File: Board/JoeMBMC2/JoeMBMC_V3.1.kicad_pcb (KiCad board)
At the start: 2 copper layers, 68 x 92 mm, 73 parts, among them J1 5007620481, J2 CAN2_T, J3 CAN1_T, Q1 BSO615NG, Q2 BSO615NG, Q3 P-Chanel Mosfet, U1 Teensy4.0, U2 SN65HVD230, U3 DCDC 5V, U4 IS281-4, U5 SN65HVD230, U6 DCDC 3.3V, U7 Level Shifter 5V to 3V, U8 Level Shifter 5V to 3V

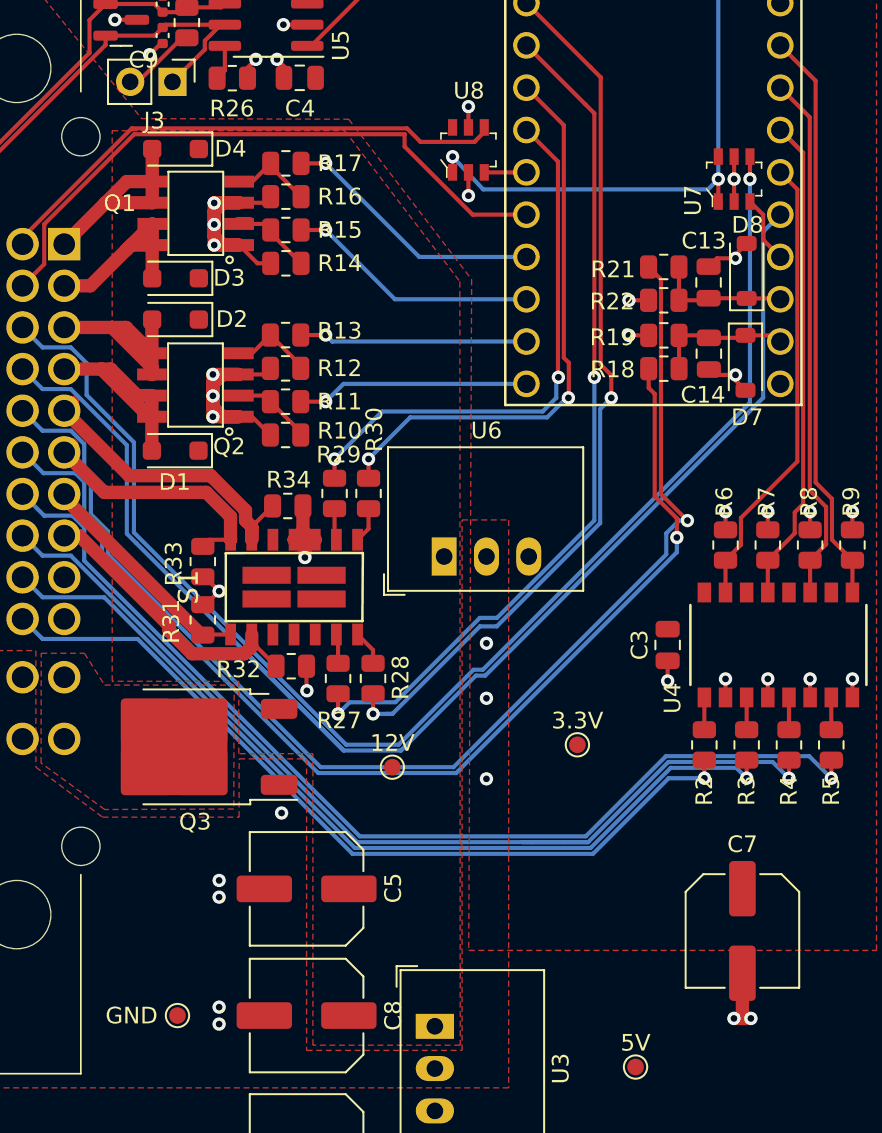
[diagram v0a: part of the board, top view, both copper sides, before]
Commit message: remove zener on analogue sensor inputs
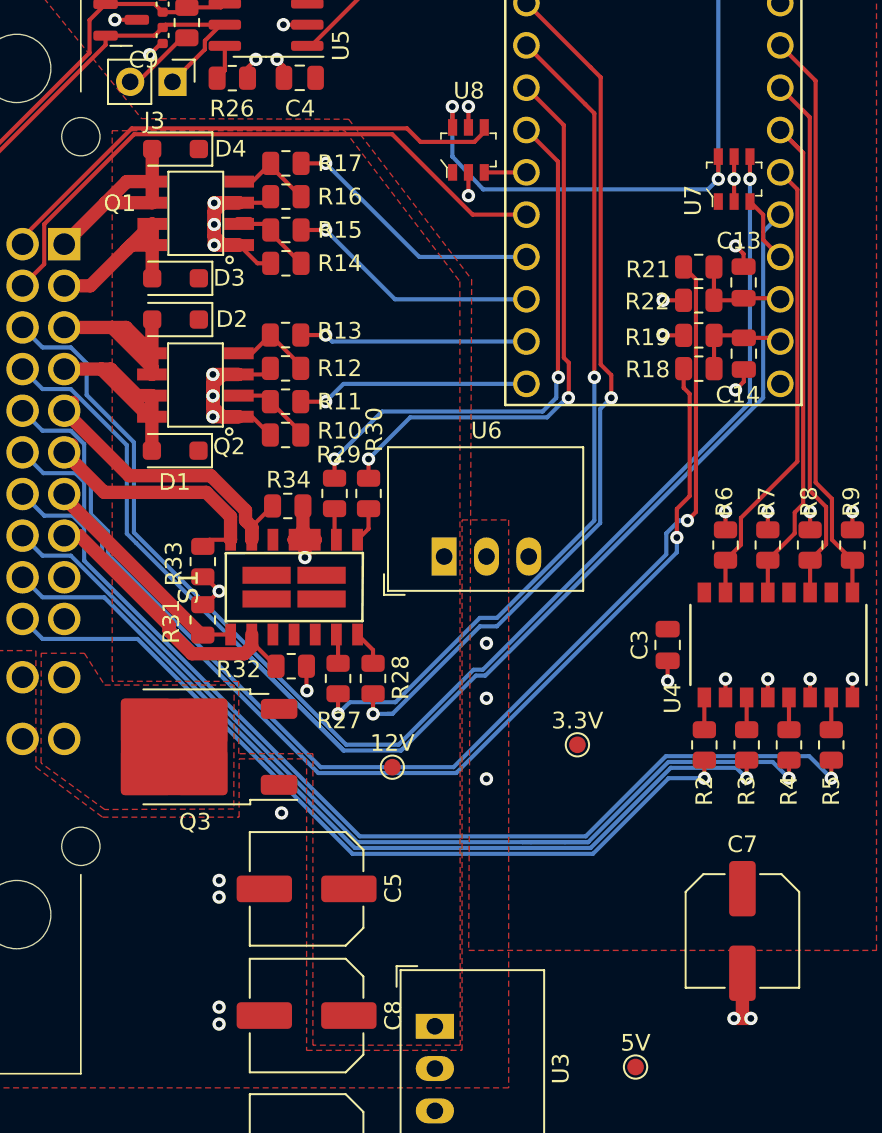
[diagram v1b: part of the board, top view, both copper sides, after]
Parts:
- removed D7, D8: D_Zener, Diode_SMD:D_SOD-123
- removed GND: TestPoint_Pad_D1.0mm, TestPoint:TestPoint_Pad_D1.0mm
- moved C13 2.10 mm to (153.5, 77.4)
- moved R18 2.10 mm to (150.8, 82.6)
- moved R19 2.10 mm to (150.8, 80.6)
- moved C14 2.10 mm to (153.5, 81.7)
- moved R21 2.10 mm to (150.8, 76.5)
- moved R22 2.10 mm to (150.8, 78.5)
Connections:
- U7 pad 1: +5V -> +3V3
- U7 pad 6: +3V3 -> +5V
- U8 pad 1: +5V -> +3V3
- U8 pad 6: +3V3 -> +5V
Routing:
- net +5V: track 41.7 -> 44.9 mm
- net GND: track 87.3 -> 84.3 mm
- net Teensy_ASEN1: track 8.16 -> 6.06 mm
- net Teensy_ASEN2: track 8.35 -> 6.66 mm
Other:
- board text added: "JoeMBMC V3.1"
- board text removed: "JoeMBMS V3.1"
